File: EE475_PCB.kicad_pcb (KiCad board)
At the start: 2 copper layers, 11 parts, among them J1 Conn_01x15_Female, J2 Conn_01x02_Female, J3 Conn_01x15_Female, J4 Conn_01x02_Female, Q1 S8050, Q2 S8050

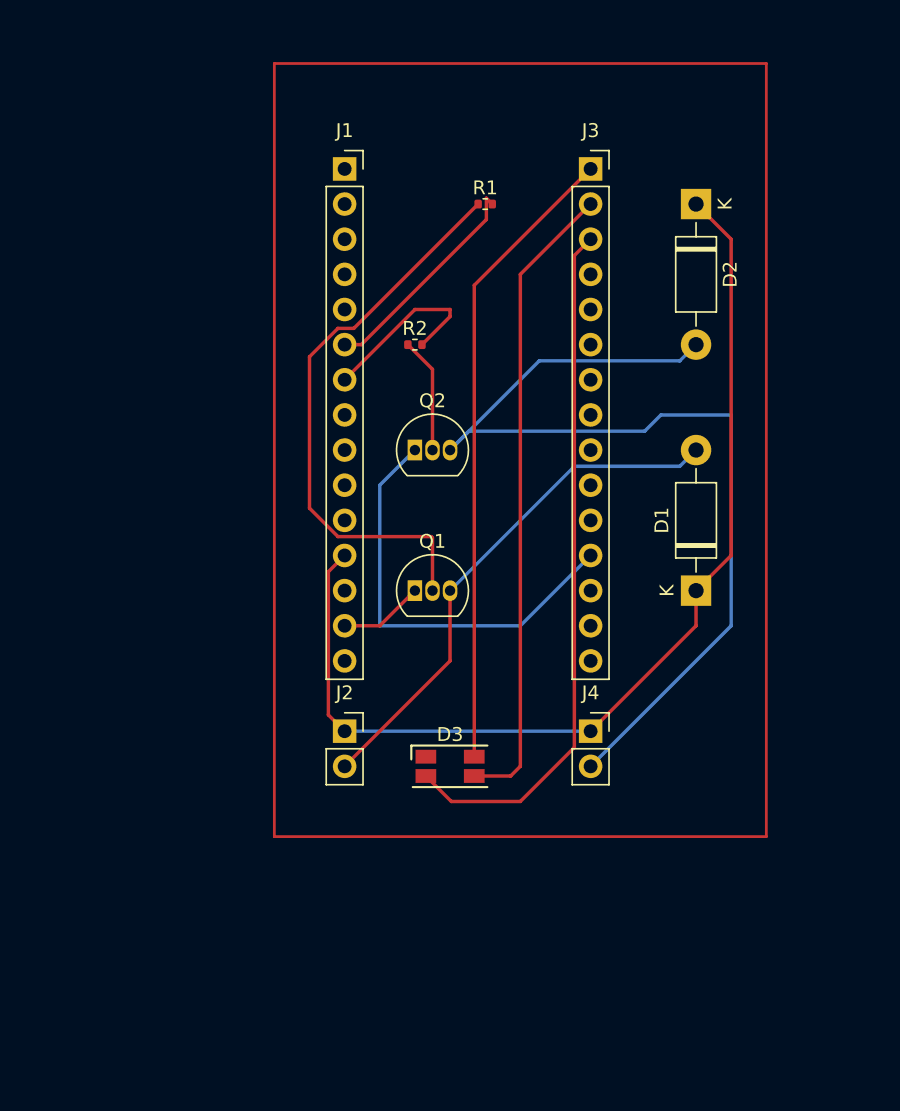
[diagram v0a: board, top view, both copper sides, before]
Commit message: Updated Schematic of motor hub with power supply width
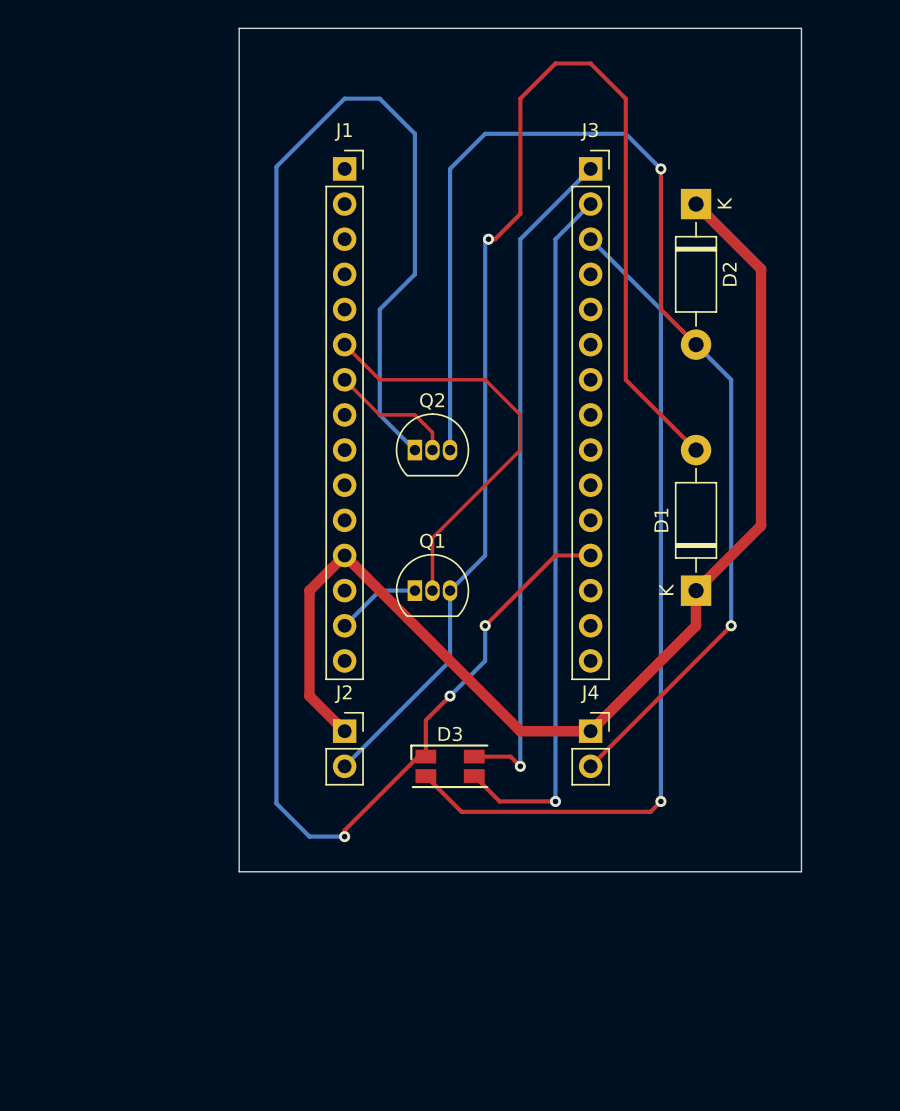
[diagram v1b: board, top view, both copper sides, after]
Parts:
- removed R1, R2: 5k, Resistor_SMD:R_0402_1005Metric
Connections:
- Q1 pad 2: Net-(Q1-Pad2) -> Net-(J1-Pad6)
- Q2 pad 2: Net-(Q2-Pad2) -> /pwm_7
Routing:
- net Net-(D3-Pad1): track 31.1 -> 119.5 mm, vias 0 -> 3
- net Net-(D1-Pad2): track 37.8 -> 91.0 mm, vias 0 -> 1
- net Net-(Q1-Pad2): track 41.3 -> 0.00 mm
- net Net-(D2-Pad2): track 71.9 -> 87.2 mm, vias 0 -> 2
- net Net-(J1-Pad6): track 16.1 -> 30.1 mm
- net Net-(D3-Pad2): track 50.3 -> 61.1 mm, vias 0 -> 1
- net Net-(Q2-Pad2): track 8.36 -> 0.00 mm
- net Net-(D1-Pad1): track 74.8 -> 83.0 mm
- net Net-(D3-Pad3): track 46.4 -> 50.9 mm, vias 0 -> 1
- net /pwm_7: track 13.1 -> 9.20 mm
- net Net-(D3-Pad4): track 46.0 -> 48.9 mm, vias 0 -> 1
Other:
- board outline added: 40.6 x 61 mm

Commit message: Final design of the PCB baord for Motor Controller
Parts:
- added J5: Conn_01x02_Female, Connector_PinSocket_2.54mm:PinSocket_1x02_P2.54mm_Vertical, F.Cu at (162.6, 121.9)
- added J6: Conn_01x02_Female, Connector_PinSocket_2.54mm:PinSocket_1x02_P2.54mm_Vertical, F.Cu at (114.3, 121.9)
- added J7: Conn_01x02_Female, Connector_PinSocket_2.54mm:PinSocket_1x02_P2.54mm_Vertical, F.Cu at (162.6, 132.1)
- added J8: Conn_01x02_Female, Connector_PinSocket_2.54mm:PinSocket_1x02_P2.54mm_Vertical, F.Cu at (114.3, 132.1)
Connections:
- J1 pad 12: Net-(D1-Pad1) -> unconnected-(J1-Pad12)
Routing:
- net Net-(D1-Pad1): track 83.0 -> 146.3 mm
- net Net-(J1-Pad14): track 6.13 -> 67.7 mm, vias 0 -> 1
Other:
- board size 40.6 x 61 mm -> 61 x 76.2 mm
- board text added: "Haptic Feedback Controller"

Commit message: Updated version of the PCB based on professor and TAs feedback
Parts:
- added R1: 1k, Resistor_SMD:R_0402_1005Metric, F.Cu at (142.2, 81.3)
- added R2: 1k, Resistor_SMD:R_0402_1005Metric, F.Cu at (144.8, 78.7)
- added R3: 1k, Resistor_SMD:R_0402_1005Metric, F.Cu at (147.3, 119.4)
- D3: value LED_ABGR -> LED_BGRK
- moved Q2 14.8 mm to (121.9, 83.8)
- moved Q1 13.0 mm to (121.9, 99.1)
- moved J1 2.54 mm to (132.1, 71.1)
- moved D3 2.54 mm to (137.2, 116.8), turned to 180 degrees
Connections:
- J1 pad 14: Net-(J1-Pad14) -> Net-(D3-Pad4)
- J3 pad 1: Net-(D3-Pad4) -> Net-(J3-Pad1)
- J3 pad 12: Net-(D3-Pad1) -> unconnected-(J3-Pad12)
- J3 pad 2: Net-(D3-Pad3) -> Net-(J3-Pad2)
- J3 pad 3: Net-(D3-Pad2) -> Net-(J3-Pad3)
- J5 pad 2: Net-(J1-Pad14) -> Net-(D3-Pad4)
- J6 pad 2: Net-(J1-Pad14) -> Net-(D3-Pad4)
- Q1 pad 1: Net-(J1-Pad14) -> Net-(D3-Pad4)
- Q2 pad 1: Net-(D3-Pad1) -> Net-(D3-Pad4)
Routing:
- net Net-(D3-Pad1): track 119.5 -> 9.06 mm, vias 3 -> 0
- net Net-(J1-Pad14): track 67.7 -> 0.00 mm, vias 1 -> 0
- net Net-(D3-Pad4): track 48.9 -> 106.3 mm, vias 1 -> 2
- net Net-(J3-Pad3): track 0.00 -> 48.4 mm, vias 0 -> 1
- net Net-(D1-Pad2): track 91.0 -> 119.1 mm, vias 1 -> 2
- net Net-(D3-Pad2): track 61.1 -> 39.3 mm, vias 1 -> 0
- net Net-(D3-Pad3): track 50.9 -> 37.2 mm, vias 1 -> 0
- net Net-(J3-Pad1): track 0.00 -> 12.2 mm
- net Net-(J1-Pad6): track 30.1 -> 20.4 mm, vias 0 -> 1
- net Net-(J3-Pad2): track 0.00 -> 5.62 mm
- net Net-(D2-Pad2): track 87.2 -> 92.2 mm, vias 2 -> 3
- net /pwm_7: track 9.20 -> 10.7 mm

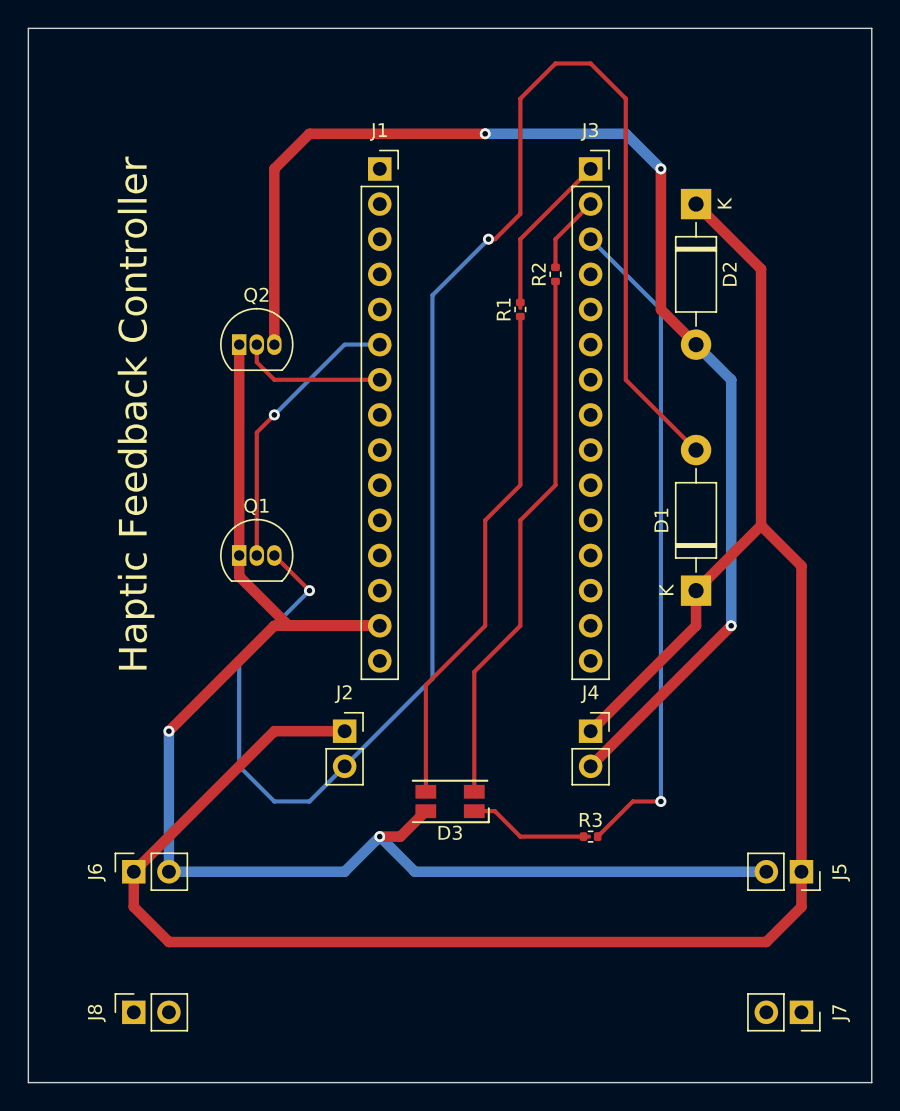
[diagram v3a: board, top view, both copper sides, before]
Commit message: Modify LED and resistor footprint
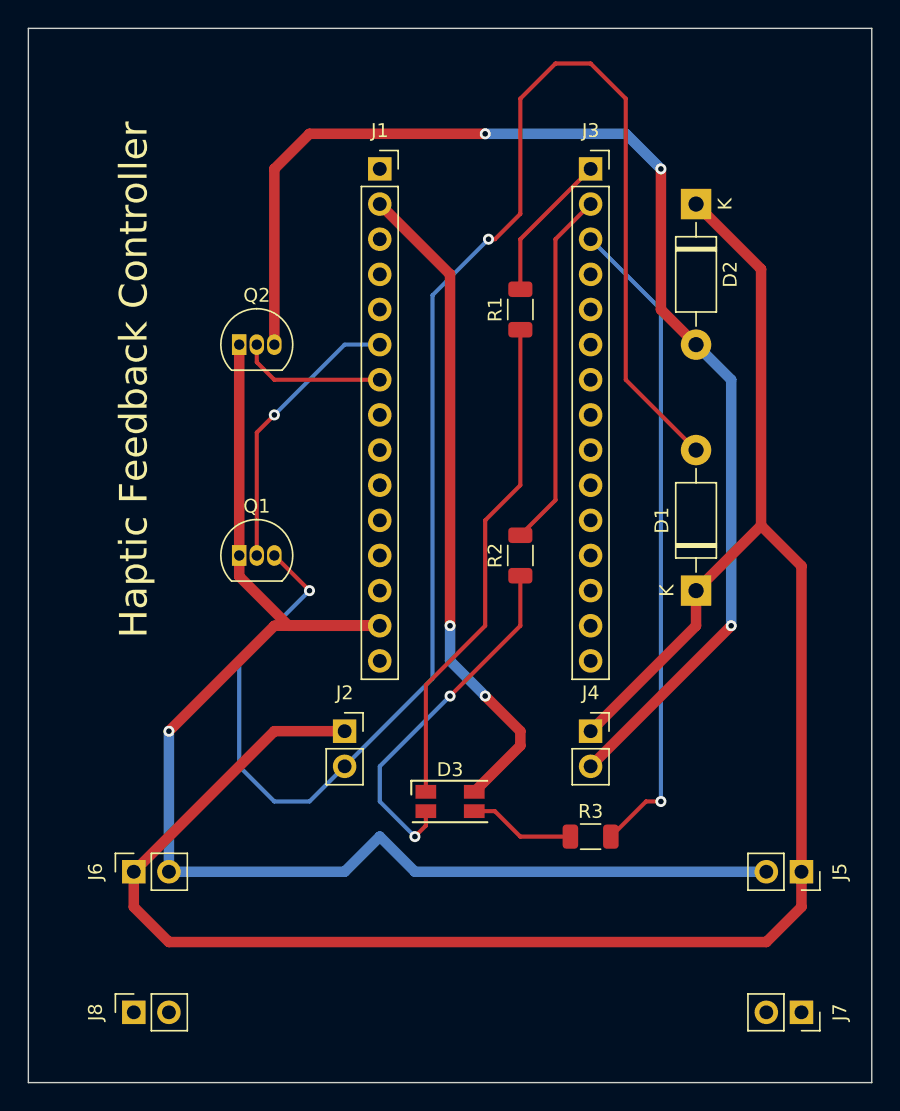
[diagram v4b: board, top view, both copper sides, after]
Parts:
- D3: value LED_BGRK -> LED_RGBA
- R1, R2, R3: footprint Resistor_SMD:R_0402_1005Metric -> Resistor_SMD:R_1206_3216Metric
- moved R2 20.5 mm to (142.2, 99.1)
- turned D3 to 0 degrees
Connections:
- D3 pad 1: Net-(D3-Pad1) -> Net-(R1-Pad1)
- D3 pad 3: Net-(D3-Pad3) -> Net-(R3-Pad1)
- D3 pad 4: Net-(D3-Pad4) -> Net-(J1-Pad2)
- J1 pad 14: Net-(D3-Pad4) -> Net-(J1-Pad14)
- J1 pad 2: unconnected-(J1-Pad2) -> Net-(J1-Pad2)
- J5 pad 2: Net-(D3-Pad4) -> Net-(J1-Pad14)
- J6 pad 2: Net-(D3-Pad4) -> Net-(J1-Pad14)
- Q1 pad 1: Net-(D3-Pad4) -> Net-(J1-Pad14)
- Q2 pad 1: Net-(D3-Pad4) -> Net-(J1-Pad14)
- R1 pad 1: Net-(D3-Pad3) -> Net-(R1-Pad1)
- R3 pad 1: Net-(D3-Pad1) -> Net-(R3-Pad1)
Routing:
- net Net-(D3-Pad4): track 106.3 -> 0.00 mm, vias 2 -> 0
- net Net-(J1-Pad14): track 0.00 -> 102.2 mm, vias 0 -> 1
- net Net-(J1-Pad2): track 0.00 -> 48.1 mm, vias 0 -> 2
- net Net-(D3-Pad3): track 37.2 -> 0.00 mm
- net Net-(R1-Pad1): track 0.00 -> 36.2 mm
- net Net-(J3-Pad2): track 5.62 -> 26.0 mm
- net Net-(R2-Pad1): track 39.3 -> 26.3 mm, vias 0 -> 2
- net Net-(D3-Pad1): track 9.06 -> 0.00 mm
- net Net-(R3-Pad1): track 0.00 -> 7.71 mm
- net Net-(J3-Pad1): track 12.2 -> 10.8 mm
- net Net-(J3-Pad3): track 48.4 -> 47.4 mm
